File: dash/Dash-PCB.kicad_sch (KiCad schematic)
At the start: 62 parts, among them IC1 HT16K33, IC2 TLV62130ARGTT, J1 IO, J2 Conn_01x05_Pin, J5 IO, J6 IO, Q1 XP262N7002TR-G, Q2 XP262N7002TR-G, Q3 XP262N7002TR-G, Q4 XP262N7002TR-G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

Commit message: Moved connectors to the right to make more space for steering column. Made PCB Symmetrical.
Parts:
- J2: footprint Connector_Molex:Molex_Micro-Fit_3.0_43650-0515_1x05_P3.00mm_Vertical -> Connector_PinSocket_2.54mm:PinSocket_1x05_P2.54mm_Vertical
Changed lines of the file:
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@@
 			)
 		)
-		(property "Footprint" "Connector_Molex:Molex_Micro-Fit_3.0_43650-0515_1x05_P3.00mm_Vertical"
+		(property "Footprint" "Connector_PinSocket_2.54mm:PinSocket_1x05_P2.54mm_Vertical"
 			(at 130.81 219.71 0)
 			(effects

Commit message: redesign. turns out we weren't finished
Work in progress
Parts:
- removed J5, J6: IO, Connector_Molex:Molex_Micro-Fit_3.0_43045-1200_2x06_P3.00mm_Horizontal, symbol Connector_Generic:Conn_02x06_Top_Bottom
- added C10, C11: 10p, Capacitor_SMD:C_0603_1608Metric_Pad1.08x0.95mm_HandSolder, symbol Device:C
- added H10, H11, H12, H5, H6, H7, H8, H9: MountingHole, MountingHole:MountingHole_3.2mm_M3, symbol Mechanical:MountingHole
- added J3: Conn_02x06_Counter_Clockwise, Connector_PinHeader_2.54mm:PinHeader_2x06_P2.54mm_Vertical, symbol Connector_Generic:Conn_02x06_Counter_Clockwise
- added SP1, SP10, SP11, SP12, SP13, SP14, SP15, SP16, SP17, SP18, SP19, SP2, SP20, SP21, SP22, SP23, SP24, SP3, SP4, SP5, SP6, SP7, SP8, SP9: Solder Pad, TestPoint:TestPoint_Pad_D2.0mm, symbol Connector:TestPoint
- added Y1: 20MHz, Crystal:Crystal_SMD_SeikoEpson_FA128-4Pin_2.0x1.6mm, symbol Device:Crystal_GND24
- R10, R7, R8: value 10k -> 1K
- R12, R3, R4: value 1K -> 10k
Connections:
- net +12V: now also R10.1, R7.1, SP13.1, SP14.1; no longer R11.1, R3.1
- net B0: now also J3.9 (Pin_9)
- net B1: now also J3.10 (Pin_10)
- net B2: now also J3.11 (Pin_11)
- net B5: now also J3.12 (Pin_12)
- net BUTTON_R2D: now also SP20.1
- net BUTTON_SELF_DESTRUCT+: now also SP15.1
- net BUTTON_SELF_DESTRUCT-: now also SP21.1
- net BUTTON_TS_ON: now also SP19.1
- net D0: now also J3.1 (Pin_1)
- net D1: now also J3.2 (Pin_2)
- net D2: now also J3.3 (Pin_3)
- net D3: now also J3.4 (Pin_4)
- net D4: now also J3.5 (Pin_5)
- net D5: now also J3.6 (Pin_6)
- net D6: now also J3.7 (Pin_7)
- net D7: now also J3.8 (Pin_8)
- net GND: now also R11.2, R3.2, C10.2, C11.2, SP7.1, Y1.2, Y1.4; no longer R10.2, R7.2
- net LED_AMS_FAULT: now also R11.1; no longer R10.1
- net LED_IMD_FAULT: now also R3.1; no longer R7.1
- net LED_R2D: now also SP10.1
- net LED_TS_OFF: now also SP9.1
- net LED_TS_ON: now also SP8.1
- net digit0: no longer U5.3 (CC)
- net digit1: no longer U4.3 (CC)
- net at Q3.3 (D), Q4.1 (G): now also R12.2; no longer R11.2
- net at Q4.3 (D): now also SP11.1
- net at R5.2: now also SP1.1
- net at R6.2: now also SP2.1
- net at Q1.3 (D), Q2.1 (G): now also R4.2; no longer R8.2
- net at R9.2: now also SP5.1
- net at Q2.3 (D): now also SP12.1
- net A6 renamed CLK+
- net CLK+: now also C10.1, Y1.3
- net A7 renamed CLK-
- net CLK-: now also C11.1, Y1.1
- new net: R7.2, SP3.1
- new net: R10.2, SP6.1
- new net: R8.2, SP4.1
- no-connect marks 54 -> 42
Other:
- note added: "Breakout portD and the rest of PortB pins for potential future use"
- note added: "Solder Pads"
- note removed: "Different combinations of resistors (R13 + R14) / pins give different button behaviours. Mount as required."

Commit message: more pcb changes
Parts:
- added H13: MountingHole, MountingHole:MountingHole_4.3mm_M4, symbol Mechanical:MountingHole
- TP1, TP2, TP3, TP4, TP5: footprint TestPoint:TestPoint_Pad_D2.5mm -> TestPoint:TestPoint_THTPad_D2.5mm_Drill1.2mm
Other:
- moved on the sheet: H1, H2, H3, H4
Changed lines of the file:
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@@
 	(rectangle
 		(start 300.99 218.44)
-		(end 330.2 248.92)
+		(end 330.2 251.46)
 		(stroke
 			(width 0)
@@
 	(text "MOUNTING HOLES"
 		(exclude_from_sim no)
-		(at 312.166 221.234 0)
+		(at 312.166 221.488 0)
 		(effects
 			(font
@@
 			)
 		)
-		(property "Footprint" "TestPoint:TestPoint_Pad_D2.5mm"
+		(property "Footprint" "TestPoint:TestPoint_THTPad_D2.5mm_Drill1.2mm"
 			(at 302.26 151.13 0)
 			(effects
@@
 	(symbol
 		(lib_id "Mechanical:MountingHole")
-		(at 303.53 228.6 0)
+		(at 303.53 232.41 0)
 		(unit 1)
 		(exclude_from_sim yes)
@@
 		(fields_autoplaced yes)
 		(property "Reference" "H4"
-			(at 306.07 227.3299 0)
+			(at 306.07 231.1399 0)
 			(effects
 				(font
@@
 		)
 		(property "Value" "MountingHole"
-			(at 306.07 229.8699 0)
+			(at 306.07 233.6799 0)
 			(effects
 				(font
@@
 		)
 		(property "Footprint" "MountingHole:MountingHole_4.3mm_M4"
-			(at 303.53 228.6 0)
+			(at 303.53 232.41 0)
 			(effects
 				(font
@@
 		)
 		(property "Datasheet" "~"
-			(at 303.53 228.6 0)
+			(at 303.53 232.41 0)
 			(effects
 				(font
@@
 		)
 		(property "Description" "Mounting Hole without connection"
-			(at 303.53 228.6 0)
+			(at 303.53 232.41 0)
 			(effects
 				(font
@@
 	)
 	(symbol
+		(lib_id "Mechanical:MountingHole")
+		(at 303.53 227.33 0)
+		(unit 1)
+		(exclude_from_sim yes)
+		(in_bom no)
+		(on_board yes)
+		(dnp no)
+		(fields_autoplaced yes)
+		(property "Reference" "H13"
+			(at 306.07 226.0599 0)
+			(effects
+				(font
+					(size 1.27 1.27)
+				)
+				(justify left)
+			)
+		)
+		(property "Value" "MountingHole"
+			(at 306.07 228.5999 0)
+			(effects
+				(font
+					(size 1.27 1.27)
+				)
+				(justify left)
+			)
+		)
+		(property "Footprint" "MountingHole:MountingHole_4.3mm_M4"
+			(at 303.53 227.33 0)
+			(effects
+				(font
+					(size 1.27 1.27)
+				)
+				(hide yes)
+			)
+		)
+		(property "Datasheet" "~"
+			(at 303.53 227.33 0)
+			(effects
+				(font
+					(size 1.27 1.27)
+				)
+				(hide yes)
+			)
+		)
+		(property "Description" "Mounting Hole without connection"
+			(at 303.53 227.33 0)
+			(effects
+				(font
+					(size 1.27 1.27)
+				)
+				(hide yes)
+			)
+		)
+		(instances
+			(project "Dash-PCB"
+				(path "/8bd0bf3b-367d-470a-bc4a-b460b6479d15"
+					(reference "H13")
+					(unit 1)
+				)
+			)
+		)
+	)
+	(symbol
 		(lib_id "Connector:TestPoint")
 		(at 219.71 237.744 270)
@@
 	(symbol
 		(lib_id "Mechanical:MountingHole")
-		(at 303.53 243.84 0)
+		(at 303.53 247.65 0)
 		(unit 1)
 		(exclude_from_sim yes)
@@
 		(fields_autoplaced yes)
 		(property "Reference" "H1"
-			(at 306.07 242.5699 0)
+			(at 306.07 246.3799 0)
 			(effects
 				(font
@@
 		)
 		(property "Value" "MountingHole"
-			(at 306.07 245.1099 0)
+			(at 306.07 248.9199 0)
 			(effects
 				(font
@@
 		)
 		(property "Footprint" "MountingHole:MountingHole_4.3mm_M4"
-			(at 303.53 243.84 0)
+			(at 303.53 247.65 0)
 			(effects
 				(font
@@
 		)
 		(property "Datasheet" "~"
-			(at 303.53 243.84 0)
+			(at 303.53 247.65 0)
 			(effects
 				(font
@@
 		)
 		(property "Description" "Mounting Hole without connection"
-			(at 303.53 243.84 0)
+			(at 303.53 247.65 0)
 			(effects
 				(font
@@
 			)
 		)
-		(property "Footprint" "TestPoint:TestPoint_Pad_D2.5mm"
+		(property "Footprint" "TestPoint:TestPoint_THTPad_D2.5mm_Drill1.2mm"
 			(at 142.24 163.83 0)
 			(effects
@@
 	(symbol
 		(lib_id "Mechanical:MountingHole")
-		(at 303.53 233.68 0)
+		(at 303.53 237.49 0)
 		(unit 1)
 		(exclude_from_sim yes)
@@
 		(fields_autoplaced yes)
 		(property "Reference" "H3"
-			(at 306.07 232.4099 0)
+			(at 306.07 236.2199 0)
 			(effects
 				(font
@@
 		)
 		(property "Value" "MountingHole"
-			(at 306.07 234.9499 0)
+			(at 306.07 238.7599 0)
 			(effects
 				(font
@@
 		)
 		(property "Footprint" "MountingHole:MountingHole_4.3mm_M4"
-			(at 303.53 233.68 0)
+			(at 303.53 237.49 0)
 			(effects
 				(font
@@
 		)
 		(property "Datasheet" "~"
-			(at 303.53 233.68 0)
+			(at 303.53 237.49 0)
 			(effects
 				(font
@@
 		)
 		(property "Description" "Mounting Hole without connection"
-			(at 303.53 233.68 0)
+			(at 303.53 237.49 0)
 			(effects
 				(font
@@
 			)
 		)
-		(property "Footprint" "TestPoint:TestPoint_Pad_D2.5mm"
+		(property "Footprint" "TestPoint:TestPoint_THTPad_D2.5mm_Drill1.2mm"
 			(at 144.78 170.18 0)
 			(effects
@@
 			)
 		)
-		(property "Footprint" "TestPoint:TestPoint_Pad_D2.5mm"
+		(property "Footprint" "TestPoint:TestPoint_THTPad_D2.5mm_Drill1.2mm"
 			(at 396.24 208.28 0)
 			(effects
@@
 			)
 		)
-		(property "Footprint" "TestPoint:TestPoint_Pad_D2.5mm"
+		(property "Footprint" "TestPoint:TestPoint_THTPad_D2.5mm_Drill1.2mm"
 			(at 151.13 186.69 0)
 			(effects
@@
 	(symbol
 		(lib_id "Mechanical:MountingHole")
-		(at 303.53 238.76 0)
+		(at 303.53 242.57 0)
 		(unit 1)
 		(exclude_from_sim yes)
@@
 		(fields_autoplaced yes)
 		(property "Reference" "H2"
-			(at 306.07 237.4899 0)
+			(at 306.07 241.2999 0)
 			(effects
 				(font
@@
 		)
 		(property "Value" "MountingHole"
-			(at 306.07 240.0299 0)
+			(at 306.07 243.8399 0)
 			(effects
 				(font
@@
 		)
 		(property "Footprint" "MountingHole:MountingHole_4.3mm_M4"
-			(at 303.53 238.76 0)
+			(at 303.53 242.57 0)
 			(effects
 				(font
@@
 		)
 		(property "Datasheet" "~"
-			(at 303.53 238.76 0)
+			(at 303.53 242.57 0)
 			(effects
 				(font
@@
 		)
 		(property "Description" "Mounting Hole without connection"
-			(at 303.53 238.76 0)
+			(at 303.53 242.57 0)
 			(effects
 				(font

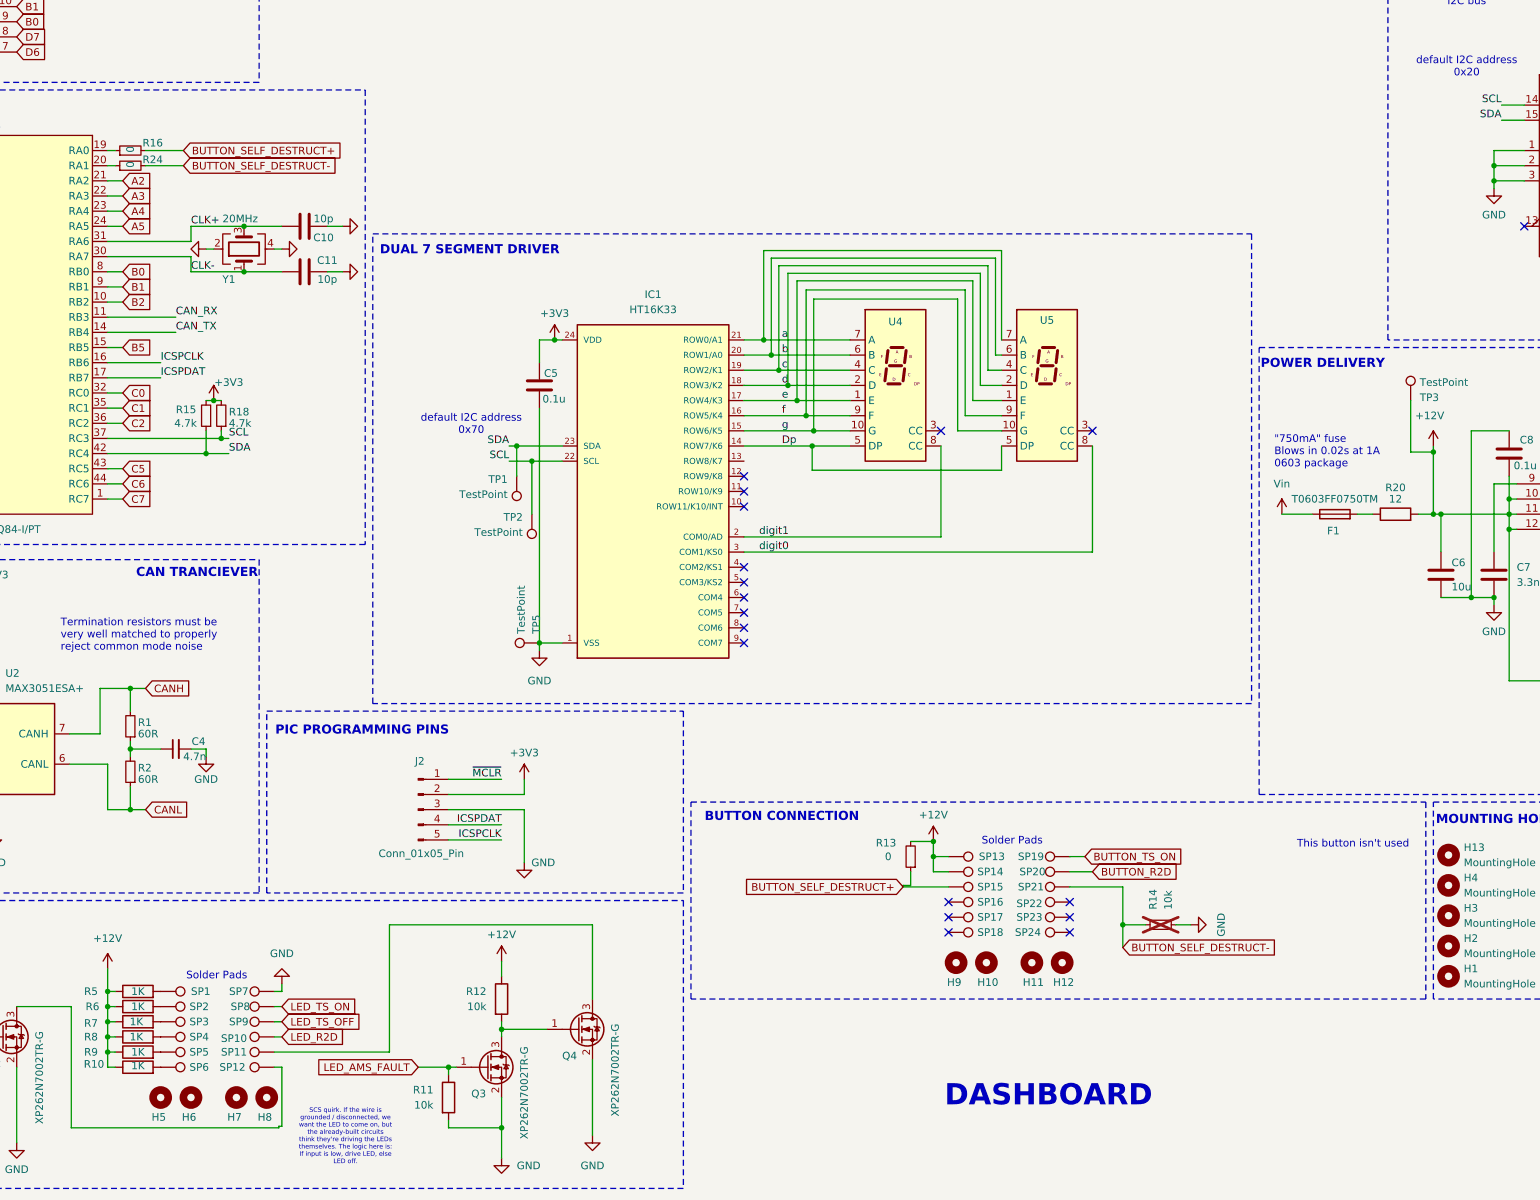
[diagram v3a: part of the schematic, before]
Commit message: Adding ziptie slots, Moving 7 seg Ic, Fixing clk and decoupling capacitors and adding debounce capacitor for button
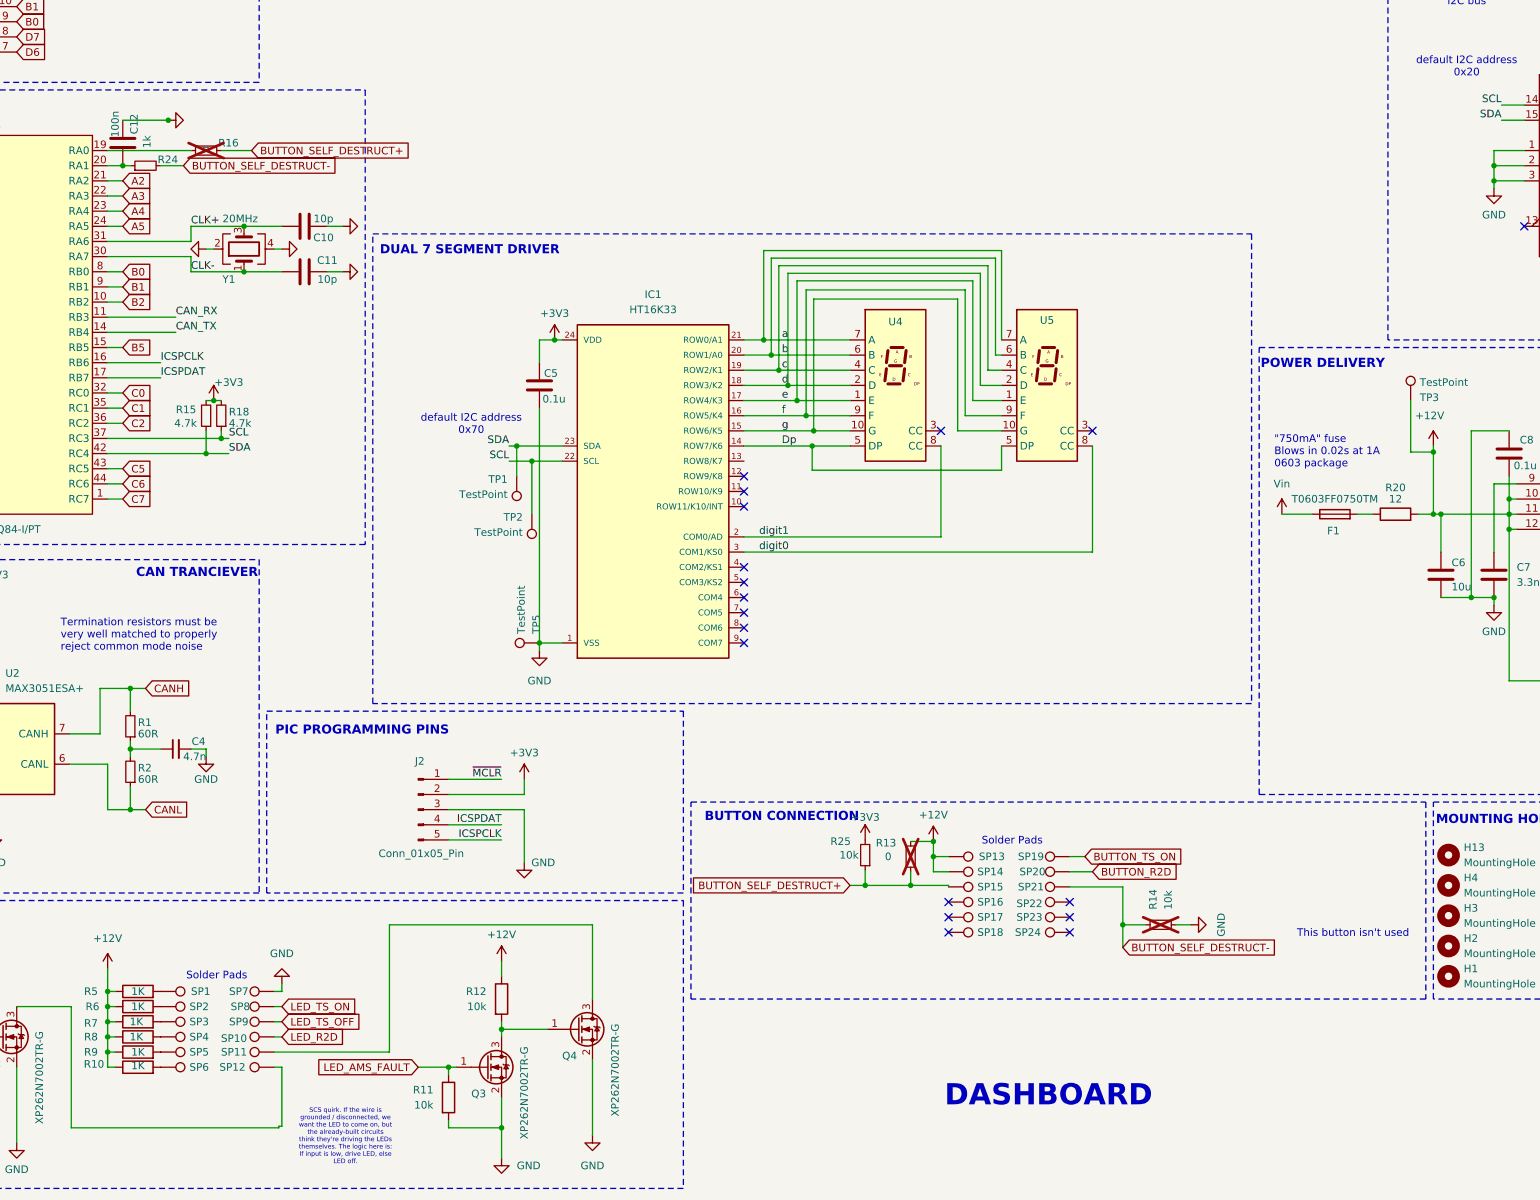
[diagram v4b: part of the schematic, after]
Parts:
- removed H10, H11, H12, H5, H6, H7, H8, H9: MountingHole, MountingHole:MountingHole_3.2mm_M3, symbol Mechanical:MountingHole
- added C12: 100n, Capacitor_SMD:C_0603_1608Metric_Pad1.08x0.95mm_HandSolder, symbol Device:C
- added R25: 10k, Resistor_SMD:R_0805_2012Metric_Pad1.20x1.40mm_HandSolder, symbol Device:R_Small
- R13, R16: now not fitted
- R24: value 0 -> 1k
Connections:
- net +3V3: now also R25.2
- net BUTTON_SELF_DESTRUCT+: now also R25.1
- net GND: now also C12.2
- net at R24.1, U1.20 (RA1): now also C12.1
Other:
- moved on the sheet: R24
